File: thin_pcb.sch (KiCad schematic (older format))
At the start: 121 parts, among them J1 USB_B_Micro, J11 Conn_01x01, J12 Conn_01x01, J13 Conn_01x01, J14 Conn_01x01, J15 Conn_01x01, J16 Conn_01x01, J17 Conn_01x01, J18 Conn_01x01, J2 AudioJack4_Ground, J21 Conn_01x07, J22 Conn_01x07, J23 Conn_01x07, J24 Conn_01x07, J25 Conn_01x07, J26 Conn_01x07, J27 Conn_01x07, J28 Conn_01x07, J3 AudioJack4_Ground, J31 Conn_01x07, J32 Conn_01x07, J33 Conn_01x07, J34 Conn_01x07, J35 Conn_01x07, J36 Conn_01x07, J37 Conn_01x07, J38 Conn_01x07, J4 Conn_02x02_Top_Bottom, J41 Conn_01x04, J42 Conn_01x04, J43 Conn_01x04, J44 Conn_01x04, J45 Conn_01x04, J46 Conn_01x04, J47 Conn_01x04, J48 Conn_01x04, J5 Conn_01x13, J51 Conn_01x01, J52 Conn_01x01, J53 Conn_01x01, J54 Conn_01x01, J55 Conn_01x01, J56 Conn_01x01, J57 Conn_01x01, J58 Conn_01x01, J6 Conn_01x03, J7 Conn_01x02, SW11 SW_Push, SW12 SW_Push, SW13 SW_Push, SW14 SW_Push, SW15 SW_Push, SW21 SW_Push, SW22 SW_Push, SW23 SW_Push, SW24 SW_Push, SW25 SW_Push, SW252 SW_Push, SW31 SW_Push, SW32 SW_Push, SW33 SW_Push, SW34 SW_Push, SW35 SW_Push, SW41 SW_Push, SW42 SW_Push, SW422 SW_Push, SW43 SW_Push, SW44 SW_Push, SW45 SW_Push, SW452 SW_Push, SW51 SW_Push, SW52 SW_Push, SW522 SW_Push, SW53 SW_Push, SW54 SW_Push, SW55 SW_Push, U1 ATmega32U4-MU, U2 USBLC6-2SC6, Y1 Crystal

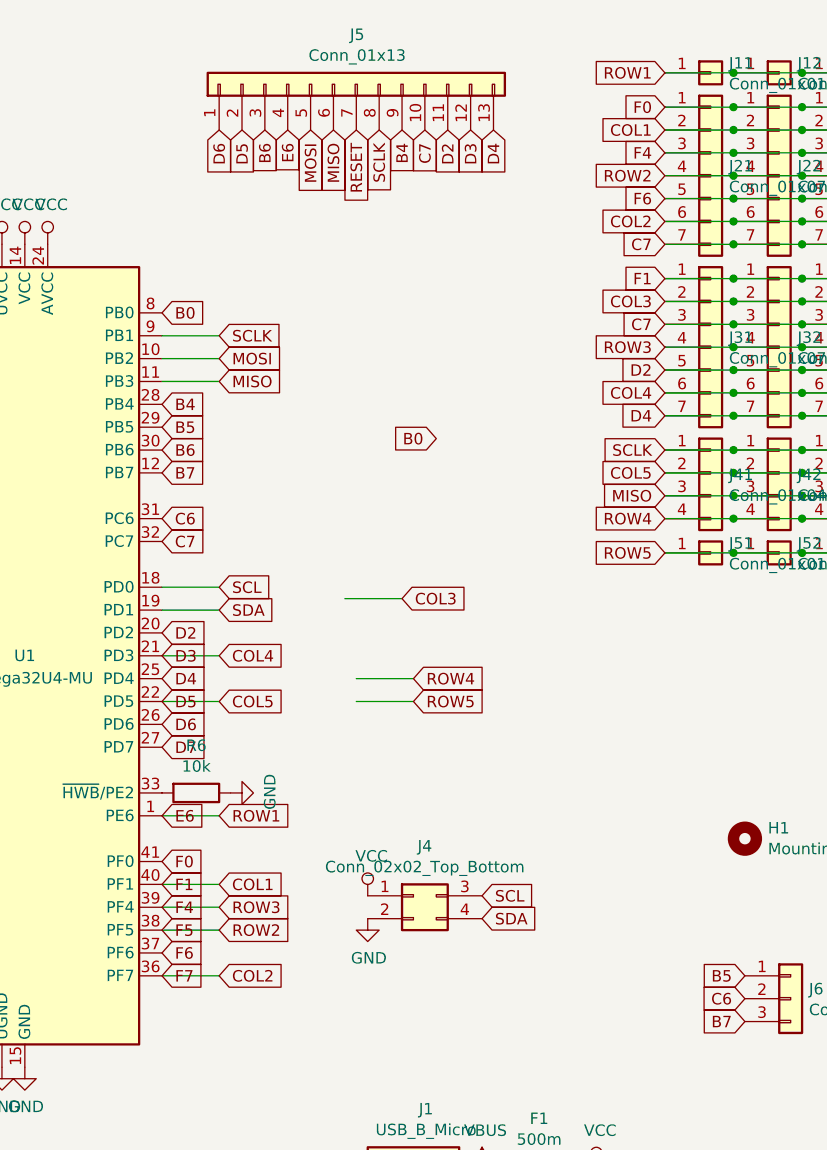
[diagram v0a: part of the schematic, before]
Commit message: spi traces
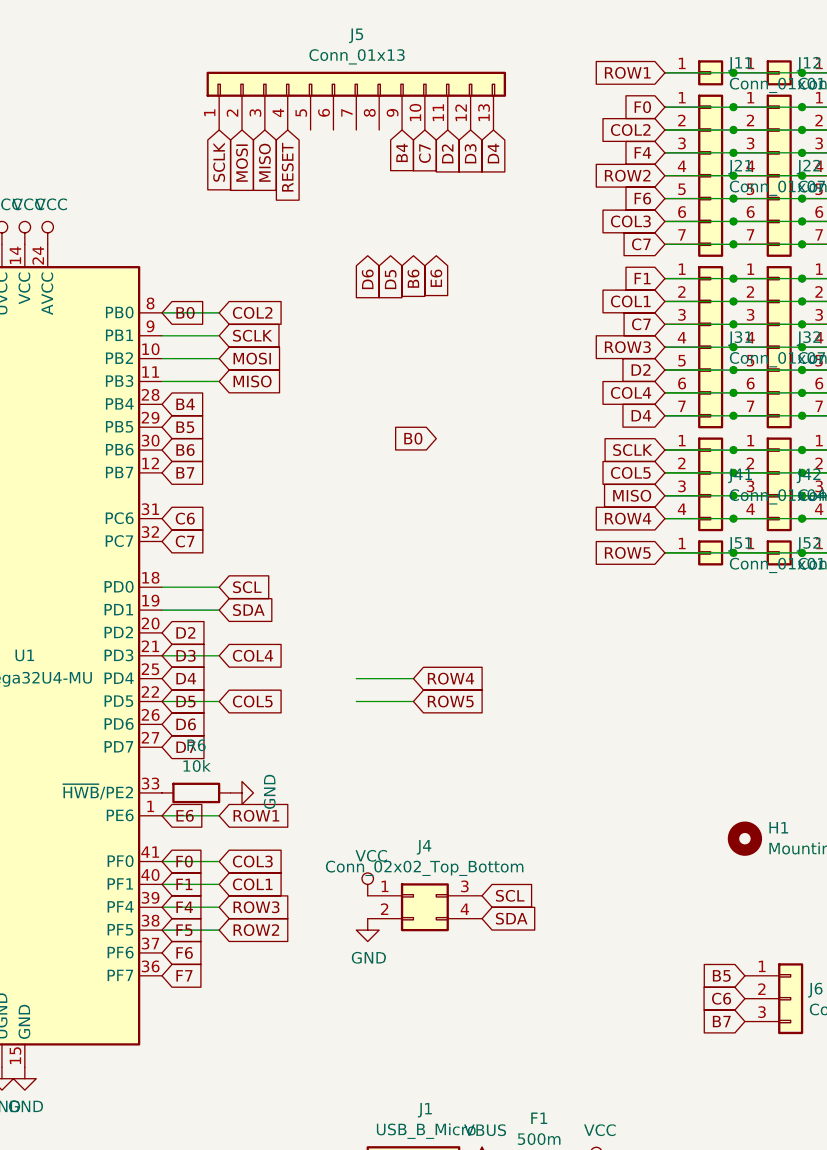
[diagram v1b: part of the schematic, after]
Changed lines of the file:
@@
 Text GLabel 9050 5700 2    50   Input ~ 0
 SCL
-Text GLabel 3000 1100 3    50   Input ~ 0
+Text GLabel 2700 1100 3    50   Input ~ 0
 MISO
-Text GLabel 2900 1100 3    50   Input ~ 0
+Text GLabel 2600 1100 3    50   Input ~ 0
 MOSI
-Text GLabel 3200 1100 3    50   Input ~ 0
+Text GLabel 2500 1100 3    50   Input ~ 0
 SCLK
 $Comp
@@
 	1    0    0    -1
 $EndComp
-Text GLabel 3100 1100 3    50   Input ~ 0
+Text GLabel 2800 1100 3    50   Input ~ 0
 RESET
 $Comp
@@
 Text GLabel 2500 4400 2    50   Input ~ 0
 COL1
-Text GLabel 2500 4800 2    50   Input ~ 0
+Text GLabel 2500 1900 2    50   Input ~ 0
 COL2
-Text GLabel 3300 3150 2    50   Input ~ 0
+Text GLabel 2500 4300 2    50   Input ~ 0
 COL3
 Text GLabel 2500 3400 2    50   Input ~ 0
@@
 	2250 4400 2500 4400
 Wire Wire Line
-	2250 4800 2500 4800
-Wire Wire Line
-	3050 3150 3300 3150
+	2250 1900 2500 1900
+Wire Wire Line
+	2250 4300 2500 4300
 Wire Wire Line
 	2250 3400 2500 3400
@@
 Wire Wire Line
 	3100 3600 3350 3600
-Text GLabel 2800 1100 3    50   Input ~ 0
+Text GLabel 3450 1650 3    50   Input ~ 0
 E6
 $Comp
@@
 Text GLabel 3650 4450 2    50   Input ~ 0
 SCL
-Text GLabel 2500 1100 3    50   Input ~ 0
+Text GLabel 3150 1650 3    50   Input ~ 0
 D6
-Text GLabel 2600 1100 3    50   Input ~ 0
+Text GLabel 3250 1650 3    50   Input ~ 0
 D5
-Text GLabel 2700 1100 3    50   Input ~ 0
+Text GLabel 3350 1650 3    50   Input ~ 0
 B6
 Text GLabel 4800 5000 0    50   Input ~ 0
@@
 Text GLabel 4450 850  0    50   Input ~ 0
 ROW1
+Text GLabel 4450 1850 0    50   Input ~ 0
+COL1
 Text GLabel 4450 1100 0    50   Input ~ 0
-COL1
+COL2
 Text GLabel 4450 1500 0    50   Input ~ 0
-COL2
-Text GLabel 4450 1850 0    50   Input ~ 0
 COL3
 Text GLabel 4450 2250 0    50   Input ~ 0

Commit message: connectors pins
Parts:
- added J01, J02, J04, J06, J07, J08: Conn_01x02, Connector_PinSocket_2.54mm:PinSocket_1x02_P2.54mm_Vertical, symbol Connector_Generic:Conn_01x02
- J11, J12, J13, J14, J15, J16, J17, J18: value Conn_01x01 -> Conn_01x03; footprint Connector_PinSocket_2.54mm:PinSocket_1x01_P2.54mm_Vertical -> Connector_PinSocket_2.54mm:PinSocket_1x03_P2.54mm_Vertical; symbol Connector_Generic:Conn_01x01 -> Connector_Generic:Conn_01x03
- J4: value Conn_02x02_Top_Bottom -> Conn_01x06; footprint Connector_PinSocket_2.54mm:PinSocket_2x02_P2.54mm_Vertical -> Connector_PinSocket_2.54mm:PinSocket_1x06_P2.54mm_Vertical; symbol Connector_Generic:Conn_02x02_Top_Bottom -> Connector_Generic:Conn_01x06
- J41, J42, J43, J44, J45, J46, J47, J48: footprint Connector_PinSocket_2.54mm:PinSocket_1x04_P2.54mm_Vertical -> Connector_PinSocket_2.54mm:PinSocket_1x07_P2.54mm_Vertical; symbol Connector_Generic:Conn_01x04 -> Connector_Generic:Conn_01x07
- J5: value Conn_01x13 -> Conn_01x06; footprint Connector_PinSocket_2.54mm:PinSocket_1x13_P2.54mm_Vertical -> Connector_PinSocket_2.54mm:PinSocket_1x06_P2.54mm_Vertical; symbol Connector_Generic:Conn_01x13 -> Connector_Generic:Conn_01x06
- J6: value Conn_01x03 -> Conn_02x02; footprint Connector_PinSocket_2.54mm:PinSocket_1x03_P2.54mm_Vertical -> Connector_PinSocket_2.54mm:PinSocket_2x02_P2.54mm_Vertical; symbol Connector_Generic:Conn_01x03 -> Connector_Generic:Conn_02x02_Top_Bottom
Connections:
- wire segments 244 -> 289
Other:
- moved on the sheet: C1, C2, H1, J21, J22, J23, J24, J25, J26, J27, J28, J31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

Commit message: draft
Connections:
- wire segments 289 -> 288
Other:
- moved on the sheet: J4, J5, J6
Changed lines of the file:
@@
 Text GLabel 9050 5700 2    50   Input ~ 0
 SCL
-Text GLabel 5150 4800 3    50   Input ~ 0
+Text GLabel 5100 4550 3    50   Input ~ 0
 MISO
-Text GLabel 5050 4800 3    50   Input ~ 0
+Text GLabel 5000 4550 3    50   Input ~ 0
 MOSI
-Text GLabel 4950 4800 3    50   Input ~ 0
+Text GLabel 4900 4550 3    50   Input ~ 0
 SCLK
-Text GLabel 5250 4800 3    50   Input ~ 0
+Text GLabel 5200 4550 3    50   Input ~ 0
 RESET
 $Comp
@@
 	0    -1   -1   0
 $EndComp
-Text GLabel 2500 4400 2    50   Input ~ 0
+Text GLabel 2500 2300 2    50   Input ~ 0
 COL1
 Text GLabel 2500 1900 2    50   Input ~ 0
 COL2
-Text GLabel 2500 4300 2    50   Input ~ 0
+Text GLabel 2500 4400 2    50   Input ~ 0
 COL3
-Text GLabel 3450 3900 2    50   Input ~ 0
+Text GLabel 2500 3600 2    50   Input ~ 0
 COL4
-Text GLabel 3450 4100 2    50   Input ~ 0
+Text GLabel 2750 2100 2    50   Input ~ 0
 COL5
 Text GLabel 2500 4100 2    50   Input ~ 0
 ROW1
-Text GLabel 2500 4600 2    50   Input ~ 0
+Text GLabel 2500 4500 2    50   Input ~ 0
 ROW2
-Text GLabel 2500 4500 2    50   Input ~ 0
+Text GLabel 2500 3700 2    50   Input ~ 0
 ROW3
-Text GLabel 3350 3500 2    50   Input ~ 0
+Text GLabel 2500 3300 2    50   Input ~ 0
 ROW4
-Text GLabel 3350 3600 2    50   Input ~ 0
+Text GLabel 2500 2500 2    50   Input ~ 0
 ROW5
 Text GLabel 2250 1900 2    50   Input ~ 0
@@
 	2250 1900 2500 1900
 Wire Wire Line
-	2250 4300 2500 4300
-Wire Wire Line
-	3200 3900 3450 3900
+	2250 2300 2500 2300
+Wire Wire Line
+	2250 3600 2500 3600
 Text GLabel 2250 3400 2    50   Input ~ 0
 D3
@@
 F7
 Wire Wire Line
-	3200 4100 3450 4100
-Wire Wire Line
 	2250 4100 2500 4100
 Wire Wire Line
-	2250 4600 2500 4600
-Wire Wire Line
 	2250 4500 2500 4500
 Wire Wire Line
-	3100 3500 3350 3500
-Wire Wire Line
-	3100 3600 3350 3600
-Text GLabel 3450 1650 3    50   Input ~ 0
-E6
+	2250 3700 2500 3700
+Wire Wire Line
+	2250 3300 2500 3300
+Wire Wire Line
+	2250 2500 2500 2500
 $Comp
 L power:VBUS #PWR0107
@@
 Wire Wire Line
 	2500 2000 2250 2000
-Wire Wire Line
-	2500 2100 2250 2100
 Wire Wire Line
 	2500 2200 2250 2200
@@
 L Connector_Generic:Conn_02x02_Top_Bottom J6
 U 1 1 5D135711
-P 5500 4150
-F 0 "J6" H 5580 4192 50  0000 L CNN
-F 1 "Conn_02x02" H 5580 4101 50  0000 L CNN
-F 2 "Connector_PinSocket_2.54mm:PinSocket_2x02_P2.54mm_Vertical" H 5500 4150 50  0001 C CNN
-F 3 "~" H 5500 4150 50  0001 C CNN
-	1    5500 4150
+P 5450 3900
+F 0 "J6" H 5530 3942 50  0000 L CNN
+F 1 "Conn_02x02" H 5530 3851 50  0000 L CNN
+F 2 "Connector_PinSocket_2.54mm:PinSocket_2x02_P2.54mm_Vertical" H 5450 3900 50  0001 C CNN
+F 3 "~" H 5450 3900 50  0001 C CNN
+	1    5450 3900
 	1    0    0    -1
 $EndComp
@@
 L Connector_Generic:Conn_01x06 J4
 U 1 1 5D135878
-P 5150 4600
-F 0 "J4" V 5200 4817 50  0000 C CNN
-F 1 "Conn_01x06" V 5200 4726 50  0000 C CNN
-F 2 "Connector_PinSocket_2.54mm:PinSocket_1x06_P2.54mm_Vertical" H 5150 4600 50  0001 C CNN
-F 3 "~" H 5150 4600 50  0001 C CNN
-	1    5150 4600
+P 5100 4350
+F 0 "J4" V 5150 4567 50  0000 C CNN
+F 1 "Conn_01x06" V 5150 4476 50  0000 C CNN
+F 2 "Connector_PinSocket_2.54mm:PinSocket_1x06_P2.54mm_Vertical" H 5100 4350 50  0001 C CNN
+F 3 "~" H 5100 4350 50  0001 C CNN
+	1    5100 4350
 	0    -1   -1   0
 $EndComp
@@
 L Connector_Generic:Conn_01x06 J5
 U 1 1 5D141D0D
-P 5800 4600
-F 0 "J5" V 6017 4596 50  0000 C CNN
-F 1 "Conn_01x06" V 5926 4596 50  0000 C CNN
-F 2 "Connector_PinSocket_2.54mm:PinSocket_1x06_P2.54mm_Vertical" H 5800 4600 50  0001 C CNN
-F 3 "~" H 5800 4600 50  0001 C CNN
-	1    5800 4600
-	0    -1   -1   0
-$EndComp
-Text GLabel 3150 1650 3    50   Input ~ 0
-D6
-Text GLabel 3250 1650 3    50   Input ~ 0
-D5
-Text GLabel 3350 1650 3    50   Input ~ 0
-B6
+P 5750 4350
+F 0 "J5" V 5967 4346 50  0000 C CNN
+F 1 "Conn_01x06" V 5876 4346 50  0000 C CNN
+F 2 "Connector_PinSocket_2.54mm:PinSocket_1x06_P2.54mm_Vertical" H 5750 4350 50  0001 C CNN
+F 3 "~" H 5750 4350 50  0001 C CNN
+	1    5750 4350
+	0    -1   -1   0
+$EndComp
 Text GLabel 4450 3400 0    50   Input ~ 0
 B7
 Text GLabel 4450 3300 0    50   Input ~ 0
 C6
-Text GLabel 6750 4900 3    50   Input ~ 0
-C7
-Text GLabel 6850 4900 3    50   Input ~ 0
-D2
-Text GLabel 6950 4900 3    50   Input ~ 0
-D3
-Text GLabel 5700 4800 3    50   Input ~ 0
+Text GLabel 5650 4550 3    50   Input ~ 0
 D4
 $Comp
@@
 	1    0    0    -1
 $EndComp
-Text GLabel 3450 2450 0    50   Input ~ 0
-B0
-Text GLabel 4450 2250 0    50   Input ~ 0
-C7
-Text GLabel 4450 2450 0    50   Input ~ 0
-D2
-Text GLabel 4450 2650 0    50   Input ~ 0
-D4
-Text GLabel 4450 1500 0    50   Input ~ 0
-F4
 $Comp
 L Connector_Generic:Conn_01x07 J21
@@
 Text GLabel 4450 2900 0    50   Input ~ 0
 COL5
-Text GLabel 4450 2050 0    50   Input ~ 0
-F1
 Connection ~ 7700 1450
 Connection ~ 8000 1050
@@
 Wire Wire Line
 	9800 1450 9800 1950
-Text GLabel 6000 4800 3    50   Input ~ 0
+Text GLabel 5950 4550 3    50   Input ~ 0
 B4
 Text GLabel 4450 3200 0    50   Input ~ 0
 B5
-Text GLabel 4450 1300 0    50   Input ~ 0
+Text GLabel 4450 1500 0    50   Input ~ 0
 F0
 Text GLabel 4450 1700 0    50   Input ~ 0
 F6
-Text GLabel 4450 1900 0    50   Input ~ 0
+Text GLabel 4450 1300 0    50   Input ~ 0
 C7
 Text GLabel 4450 950  0    50   Input ~ 0
@@
 L power:GND #PWR0115
 U 1 1 5D30B159
+P 4450 700
+F 0 "#PWR0115" H 4450 450 50  0001 C CNN
+F 1 "GND" V 4455 572 50  0000 R CNN
+F 2 "" H 4450 700 50  0001 C CNN
+F 3 "" H 4450 700 50  0001 C CNN
+	1    4450 700
+	0    1    1    0
+$EndComp
+$Comp
+L power:VCC #PWR0116
+U 1 1 5D30B28B
 P 4450 800
-F 0 "#PWR0115" H 4450 550 50  0001 C CNN
-F 1 "GND" H 4455 627 50  0000 C CNN
+F 0 "#PWR0116" H 4450 650 50  0001 C CNN
+F 1 "VCC" V 4468 927 50  0000 L CNN
 F 2 "" H 4450 800 50  0001 C CNN
 F 3 "" H 4450 800 50  0001 C CNN
 	1    4450 800
-	1    0    0    -1
-$EndComp
-$Comp
-L power:VCC #PWR0116
-U 1 1 5D30B28B
-P 4450 700
-F 0 "#PWR0116" H 4450 550 50  0001 C CNN
-F 1 "VCC" H 4467 873 50  0000 C CNN
-F 2 "" H 4450 700 50  0001 C CNN
-F 3 "" H 4450 700 50  0001 C CNN
-	1    4450 700
-	1    0    0    -1
+	0    -1   -1   0
 $EndComp
 $Comp
@@
 Wire Wire Line
 	6550 700  6250 700
-Connection ~ 4450 700
 Connection ~ 4750 700
 Wire Wire Line
@@
 Wire Wire Line
 	6550 800  6250 800
-Connection ~ 4450 800
 Connection ~ 4750 800
 Wire Wire Line
@@
 Wire Wire Line
 	6250 3400 5950 3400
-Text GLabel 5800 4250 2    50   Input ~ 0
+Text GLabel 5750 4000 2    50   Input ~ 0
 B7
-Text GLabel 5800 4150 2    50   Input ~ 0
+Text GLabel 5750 3900 2    50   Input ~ 0
 C6
-Text GLabel 5300 4250 0    50   Input ~ 0
+Text GLabel 5250 4000 0    50   Input ~ 0
 B5
 Connection ~ 5950 700
@@
 Wire Wire Line
 	5350 800  5950 800
-Text GLabel 5350 4800 3    50   Input ~ 0
+Text GLabel 5300 4550 3    50   Input ~ 0
 D2
-Text GLabel 5450 4800 3    50   Input ~ 0
+Text GLabel 5400 4550 3    50   Input ~ 0
 D3
-Text GLabel 5600 4800 3    50   Input ~ 0
+Text GLabel 5550 4550 3    50   Input ~ 0
 D5
-Text GLabel 5800 4800 3    50   Input ~ 0
+Text GLabel 5750 4550 3    50   Input ~ 0
 D6
-Text GLabel 5900 4800 3    50   Input ~ 0
+Text GLabel 5850 4550 3    50   Input ~ 0
 D7
-Text GLabel 5300 4150 0    50   Input ~ 0
+Text GLabel 5250 3900 0    50   Input ~ 0
 B6
+Text GLabel 6050 4550 3    50   Input ~ 0
+F7
+Text GLabel 4450 1900 0    50   Input ~ 0
+F5
+Text GLabel 4450 2450 0    50   Input ~ 0
+D4
+Text GLabel 4450 2250 0    50   Input ~ 0
+D7
+Text GLabel 4450 2050 0    50   Input ~ 0
+F7
+Text GLabel 4450 2650 0    50   Input ~ 0
+D3
+Wire Wire Line
+	2250 2100 2750 2100
+Connection ~ 4450 800
+Connection ~ 4450 700
 $EndSCHEMATC

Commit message: arrange schema
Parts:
- renumbered J01 to J1, J02 to J2, J04 to J4, J06 to J6, J07 to J7, J08 to J8
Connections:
- wire segments 288 -> 300
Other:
- moved on the sheet: C1, C2, C3, C4, C5, C6, C7, C8, D11, D12, D13, D14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

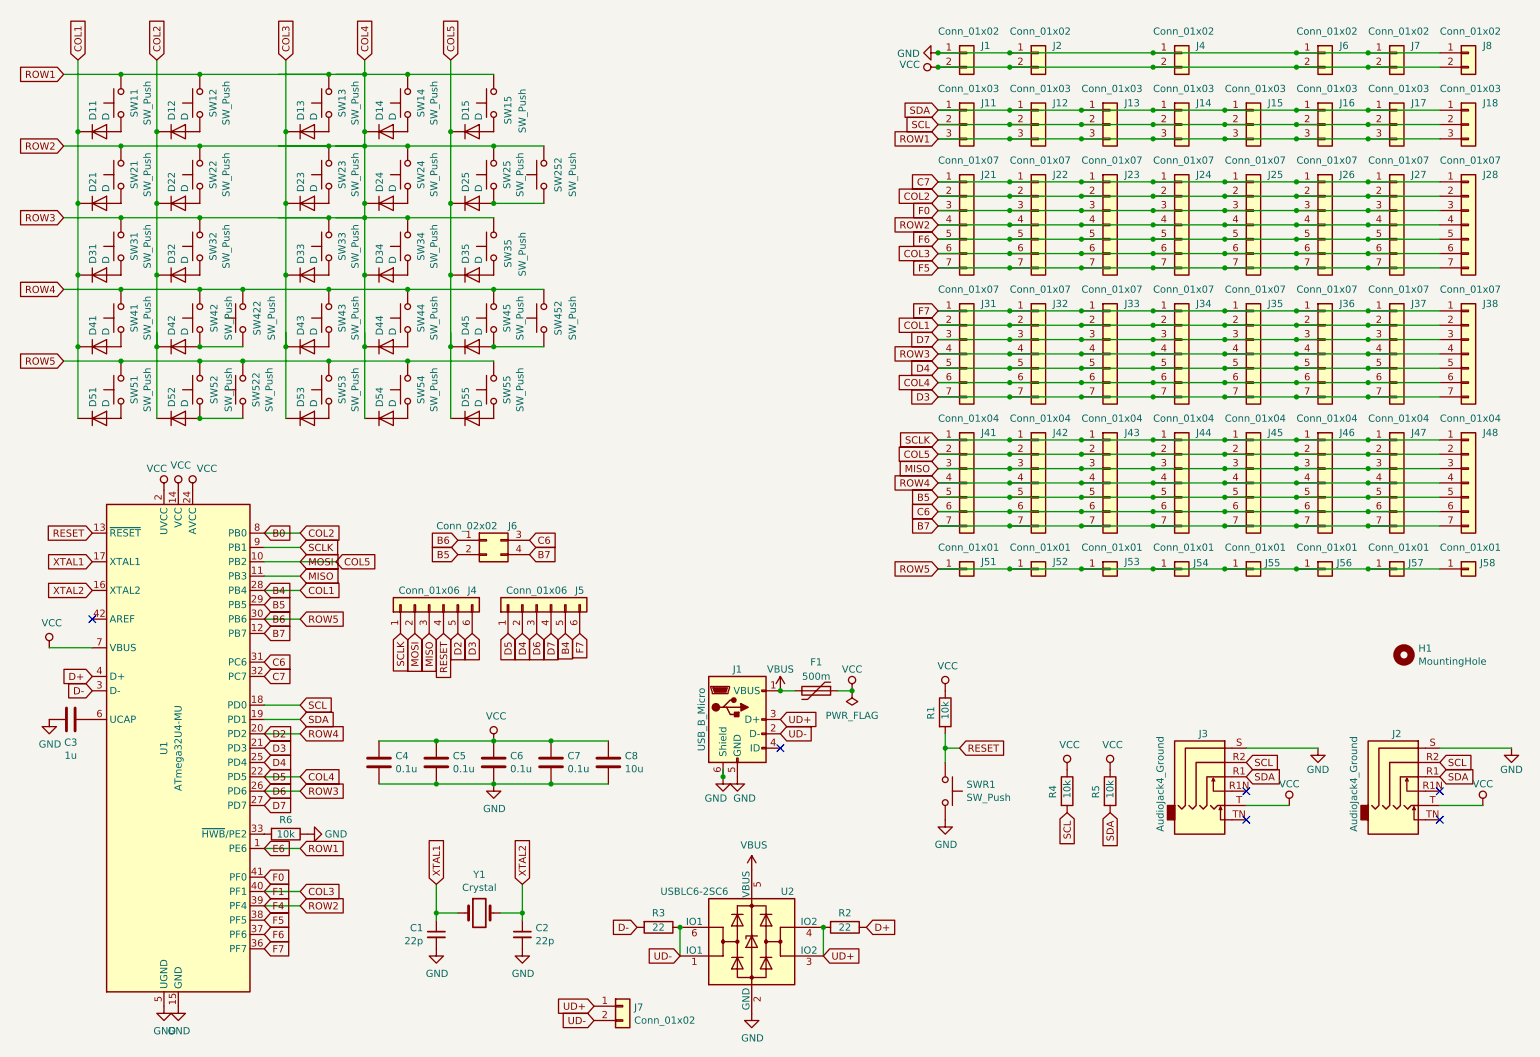
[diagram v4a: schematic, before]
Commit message: labels, mountingholes
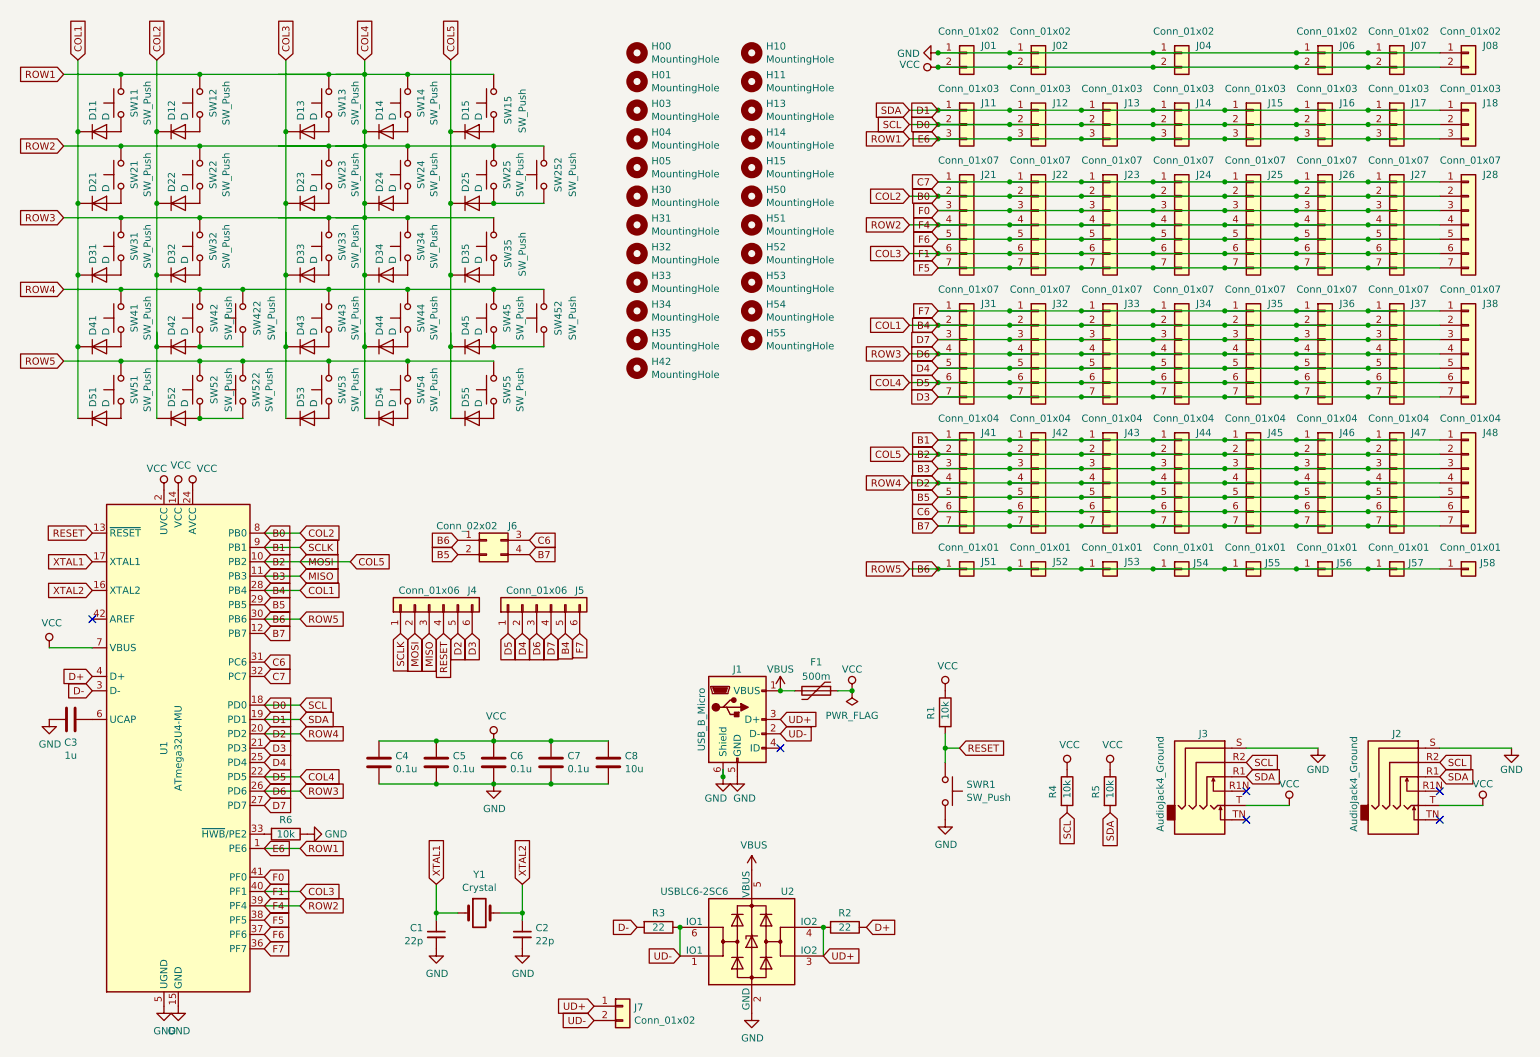
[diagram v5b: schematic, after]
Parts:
- added H01, H03, H04, H05, H10, H11, H13, H14, H15, H30, H31, H32, H33, H34, H35, H42, H50, H51, H52, H53, H54, H55: MountingHole, MountingHole:MountingHole_4mm, symbol Mechanical:MountingHole
- renumbered H1 to H00, J1 to J01, J2 to J02, J4 to J04, J6 to J06, J7 to J07, J8 to J08
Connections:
- net labels added: B1, B2, B3, D0, D1
- wire segments 300 -> 313
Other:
- moved on the sheet: H00
